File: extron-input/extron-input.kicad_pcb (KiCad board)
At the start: 2 copper layers, 92 x 37 mm, 16 parts, among them J1 SCART-F, J10 Conn_01x01, J11 Conn_01x01, J2 RED, J3 GREEN, J4 BLUE, J5 SYNC, J6 PHOENIX, J7 SENSE, J8 SENSE, J9 Conn_01x01, SW1 SW_DPDT_x2, U1 LM1881

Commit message: Oops, scart-input -> extron-input
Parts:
- J1: footprint scart-input:SCART_F_RA -> extron-input:SCART_F_RA
- J2, J3, J4, J5: footprint scart-input:BNC_90 -> extron-input:BNC_90
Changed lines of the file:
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@@
     )
   )
-  (module scart-input:BNC_90 (layer F.Cu)
+  (module extron-input:BNC_90 (layer F.Cu)
     (at 152.4 76.2 180)
     (descr "BNC connector, Tyco 1-1337543-0")
@@
     )
   )
-  (module scart-input:BNC_90 (layer F.Cu)
+  (module extron-input:BNC_90 (layer F.Cu)
     (at 132.08 76.2 180)
     (descr "BNC connector, Tyco 1-1337543-0")
@@
     )
   )
-  (module scart-input:BNC_90 (layer F.Cu)
+  (module extron-input:BNC_90 (layer F.Cu)
     (at 111.76 76.2 180)
     (descr "BNC connector, Tyco 1-1337543-0")
@@
     )
   )
-  (module scart-input:BNC_90 (layer F.Cu)
+  (module extron-input:BNC_90 (layer F.Cu)
     (at 91.44 76.2 180)
     (descr "BNC connector, Tyco 1-1337543-0")
@@
     )
   )
-  (module scart-input:SCART_F_RA (layer F.Cu)
+  (module extron-input:SCART_F_RA (layer F.Cu)
     (at 129.921 104.9655 180)
     (fp_text reference J1 (at 0.1778 -4.4577 180) (layer F.SilkS)

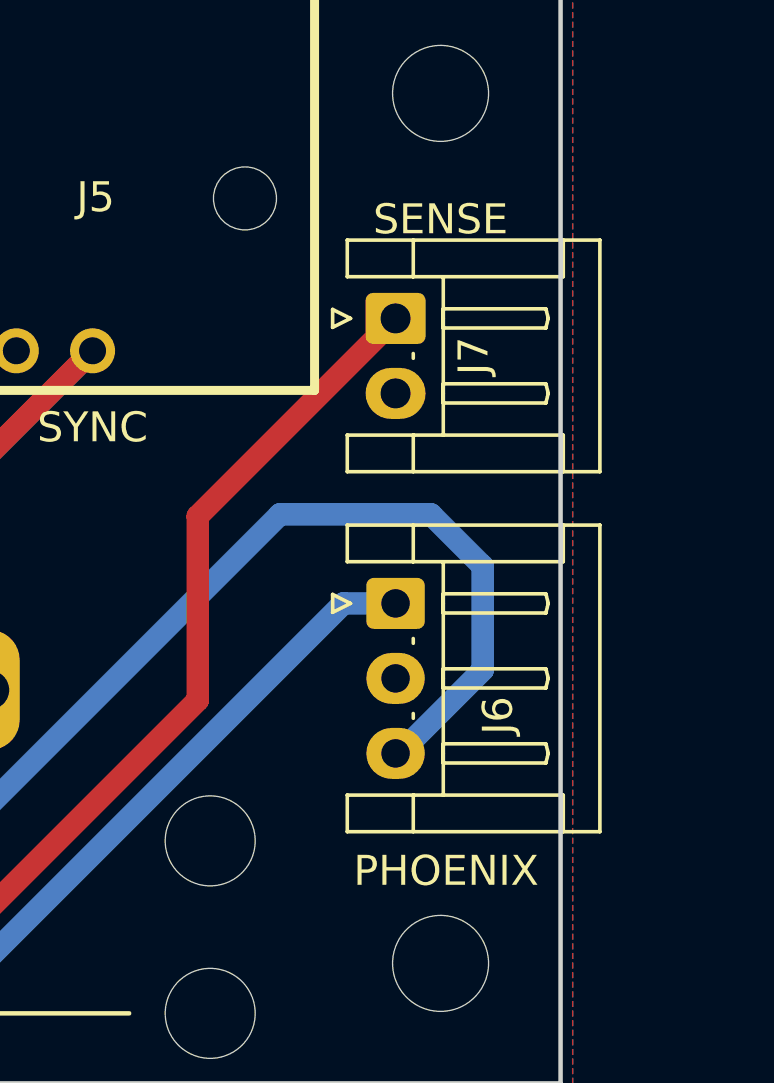
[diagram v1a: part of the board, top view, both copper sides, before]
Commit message: Random fixes to extron-input layout/schematic
There were some weirdnesses between the schematic and layout. I believe
these are fixed now.

I also switched the footprint to JST XH side connectors for both sense
and phoenix ports. I found that there are cables that can be purchased
for cheap for this form factor.
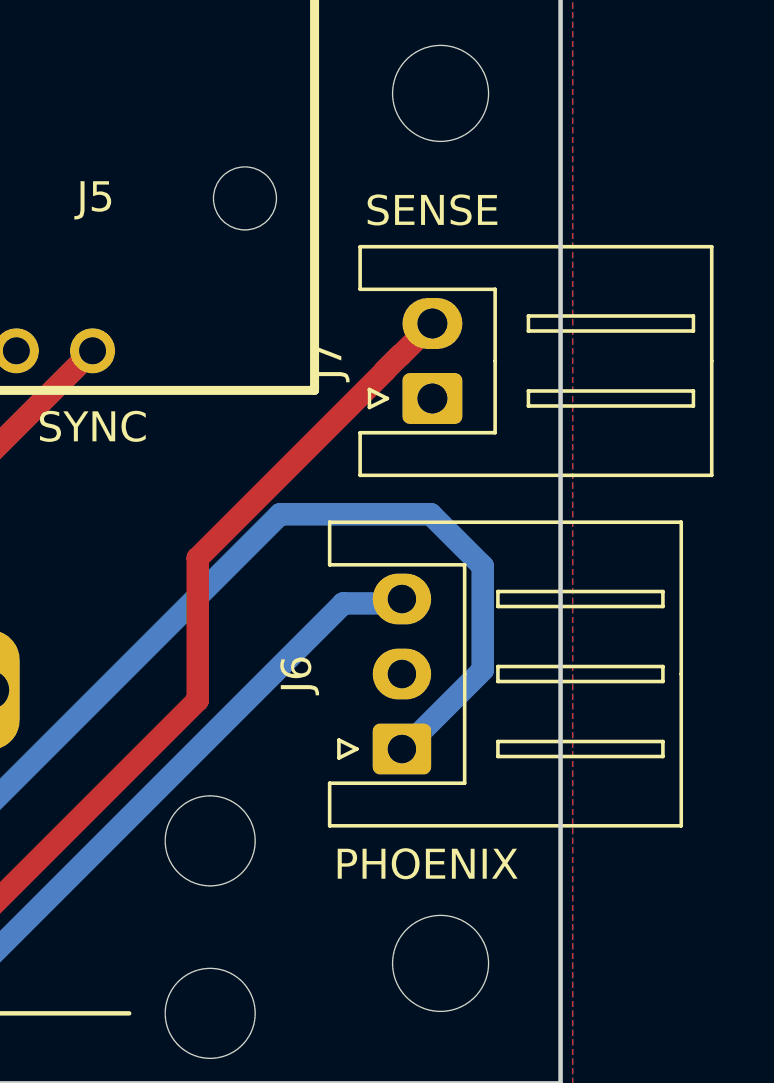
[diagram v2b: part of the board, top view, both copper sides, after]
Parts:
- J6: footprint Connector_JST:JST_EH_S03B-EH_1x03_P2.50mm_Horizontal -> Connector_JST:JST_XH_S03B-XH-A_1x03_P2.50mm_Horizontal
- J7: footprint Connector_JST:JST_EH_S02B-EH_1x02_P2.50mm_Horizontal -> Connector_JST:JST_XH_S02B-XH-A_1x02_P2.50mm_Horizontal
- J8: value SENSE -> Conn_01x01
- moved J6 4.86 mm to (162.7, 101.9), turned to 90 degrees
- moved J7 2.94 mm to (163.7, 90.2), turned to 90 degrees
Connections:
- J6 pad 1: Net-(J1-Pad6) -> Net-(J1-Pad2)
- J6 pad 3: Net-(J1-Pad2) -> Net-(J1-Pad6)
- J7 pad 1: Net-(J1-Pad8) -> GND
- J7 pad 2: GND -> Net-(J1-Pad8)

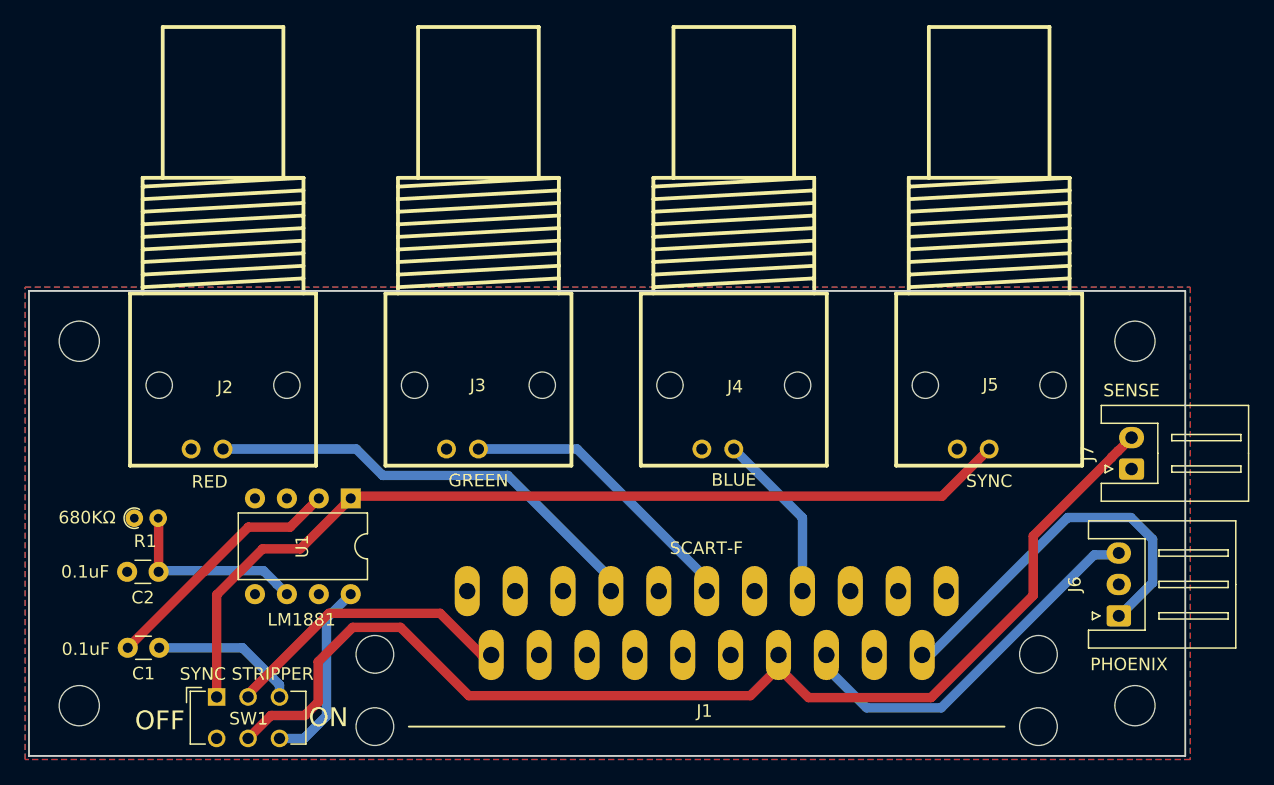
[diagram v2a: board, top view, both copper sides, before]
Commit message: Rev 2 input board (+ other small things)
BNC F -> RCA F for all outputs to extron
  The BNC is great, but expensive, and also impossible to close over an
  extron input when they are matrixed. The RCA female recepticles will
  all to use with RCA M -> BNC M adapters, which you can pre-load onto
  the extron BNC F inputs. This will allow cards to plug in
  individually, or all at once if you have a stack of cards held
  together with standoffs.

Sense circuit protection
  Added to the input board to create a 3v3 sense line to be used by an
  upcoming optional board. It also protects the SCART switch line from
  output from the optional board, just in case. This entire circuit is
  totally optional. If you're not using the upcoming sense board, then
  you can leave this unpopulated.

New footprints for 2 different types of RCA
  There's an available RCA female PCB mount footprint that I found here:
  http://smisioto.no-ip.org/elettronica/kicad/kicad-en.htm . I also
  created my own footprint for the only RCA part on lcsc.com, because if
  that one works, it's super inexpensive. You can use one or the other,
  I hope.

Gitignore added
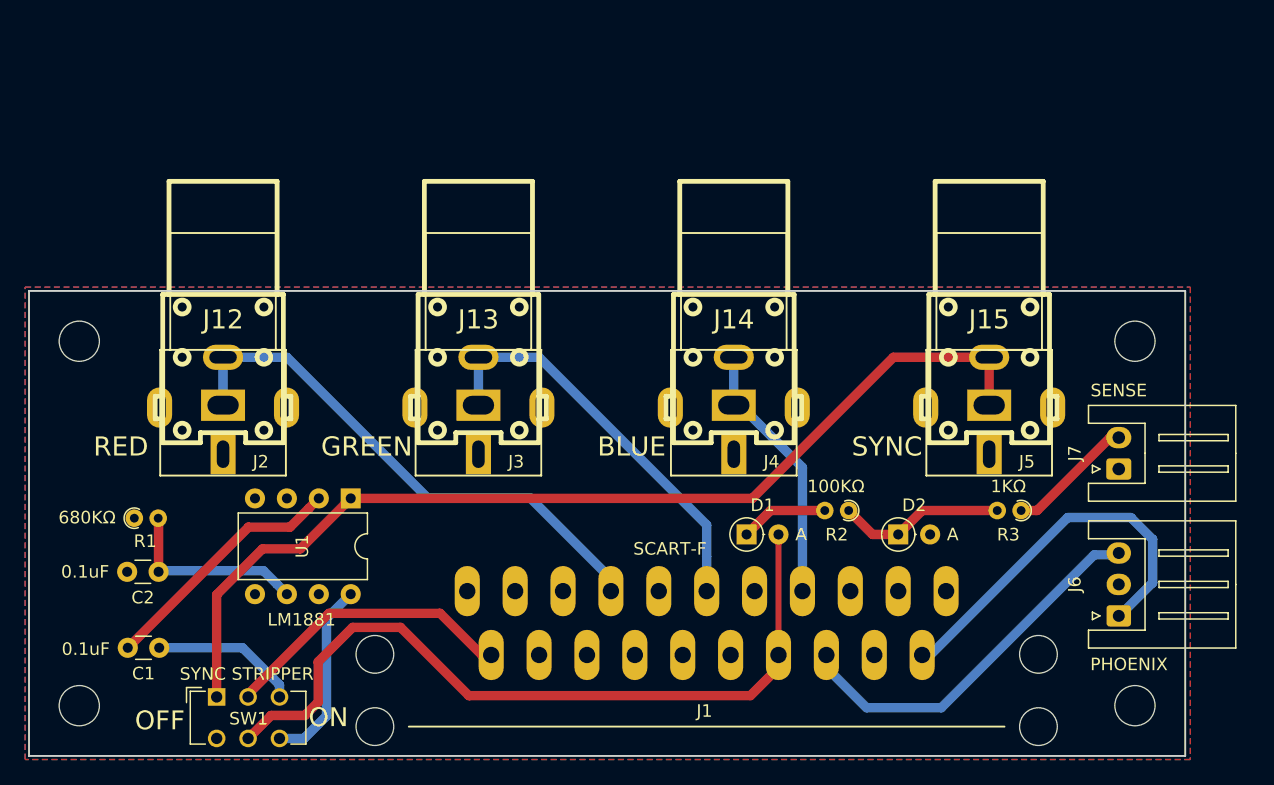
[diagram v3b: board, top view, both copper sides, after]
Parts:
- added D1: 1N4148, Diode_THT:D_DO-35_SOD27_P2.54mm_Vertical_AnodeUp, F.Cu at (133.1, 95.4)
- added D2: 1N4728A, Diode_THT:D_DO-35_SOD27_P2.54mm_Vertical_AnodeUp, F.Cu at (145.2, 95.4)
- added J12: RED, extron-input:rca_black, F.Cu at (91.4, 81.3)
- added J13: GREEN, extron-input:rca_black, F.Cu at (111.8, 81.3)
- added J14: BLUE, extron-input:rca_black, F.Cu at (132.1, 81.3)
- added J15: SYNC, extron-input:rca_black, F.Cu at (152.4, 81.3)
- added R2: 100KΩ, Resistor_THT:R_Axial_DIN0204_L3.6mm_D1.6mm_P1.90mm_Vertical, F.Cu at (141.2, 93.5)
- added R3: 1KΩ, Resistor_THT:R_Axial_DIN0204_L3.6mm_D1.6mm_P1.90mm_Vertical, F.Cu at (154.9, 93.5)
- J2, J3, J4, J5: footprint extron-input:BNC_90 -> extron-input:rca_boom
- moved J2 8.89 mm to (91.4, 85.1)
- moved J3 8.89 mm to (111.8, 85.1)
- moved J4 8.89 mm to (132.1, 85.1)
- moved J5 8.89 mm to (152.4, 85.1)
- moved J7 1.02 mm to (162.7, 90.2)
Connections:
- J1 pad 8: Net-(J1-Pad8) -> SENSE
- J7 pad 2: Net-(J1-Pad8) -> Net-(J7-Pad2)
- SW1 pad 5: Net-(J1-Pad8) -> SENSE
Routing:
- net Net-(J1-Pad8): track 92.4 -> 0.00 mm
- net SENSE: track 0.00 -> 61.5 mm
- net Net-(D2-Pad1): track 0.00 -> 13.4 mm
- net GREEN: track 23.4 -> 33.8 mm
- net Net-(J7-Pad2): track 0.00 -> 10.2 mm
- net BLUE: track 13.6 -> 20.9 mm
- net Net-(D1-Pad1): track 0.00 -> 7.01 mm
- net RED: track 36.1 -> 43.0 mm
- net SYNC: track 74.5 -> 81.2 mm
